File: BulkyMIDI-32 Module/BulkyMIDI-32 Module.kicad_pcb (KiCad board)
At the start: 2 copper layers, 100 x 100 mm, 47 parts, among them IC1 OLED, J1 DC IN, J2 MIDI OUT, J3 MIDI IN, J4 Faceplate, J5 MIDI THRU, J6 Serial, J7 Conn_Extras, J8 Module_Panel, M1 Mounting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

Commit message: Type C patched
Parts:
- added C2: 100nF, Capacitor_SMD:C_0805_2012Metric, F.Cu at (101.7, 64.9)
- added C7: 100nF, Capacitor_SMD:C_0805_2012Metric, F.Cu at (103.9, 74.4)
- added C8: 100nF, Capacitor_SMD:C_0805_2012Metric, F.Cu at (98.3, 64.9)
- added J9: USB_C_Receptacle_USB2.0, Connector_USB:USB_C_Receptacle_XKB_U262-16XN-4BVC11, F.Cu at (105.2, 58.5)
- C1, C3, C4: footprint Capacitor_THT:C_Rect_L7.0mm_W2.0mm_P5.00mm -> Capacitor_SMD:C_0805_2012Metric
- D1: value 1N4148 -> 1N4148WS; footprint Diode_THT:D_DO-35_SOD27_P7.62mm_Horizontal -> Diode_SMD:D_SOD-323
- R1, R2, R3, R4, R5, R6, R7: footprint Resistor_THT:R_Axial_DIN0207_L6.3mm_D2.5mm_P10.16mm_Horizontal -> Resistor_SMD:R_0805_2012Metric
- U1: footprint Package_DIP:DIP-14_W7.62mm -> Package_SO:SO-14_3.9x8.65mm_P1.27mm
- moved R7 9.40 mm to (113.3, 136.9)
- moved U1 8.57 mm to (159.8, 79.4)
- moved D1 1.52 mm to (132.7, 82.3)
- moved C3 1.02 mm to (120.0, 78.5)
- moved R1 0.89 mm to (167.0, 63.8)
- moved C4 0.83 mm to (109.2, 74.5)
- moved C1 0.38 mm to (149.6, 77.5)
- turned R3 to 0 degrees
- turned R4 to 0 degrees
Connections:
- A1 pad 18: (no net) -> unconnected-(A1-GPIO24-Pad18)
- A1 pad 19: (no net) -> unconnected-(A1-MOSI0/GPIO10-Pad19)
- A1 pad 21: (no net) -> unconnected-(A1-MISO0/GPIO9-Pad21)
- A1 pad 22: (no net) -> unconnected-(A1-GPIO25-Pad22)
- A1 pad 23: (no net) -> unconnected-(A1-SCLK0/GPIO11-Pad23)
- A1 pad 24: (no net) -> unconnected-(A1-~{CE0}/GPIO8-Pad24)
- A1 pad 26: (no net) -> unconnected-(A1-~{CE1}/GPIO7-Pad26)
- A1 pad 27: (no net) -> unconnected-(A1-ID_SD/GPIO0-Pad27)
- A1 pad 28: (no net) -> unconnected-(A1-ID_SC/GPIO1-Pad28)
- A1 pad 29: (no net) -> unconnected-(A1-GCLK1/GPIO5-Pad29)
- A1 pad 31: (no net) -> unconnected-(A1-GCLK2/GPIO6-Pad31)
- A1 pad 32: (no net) -> unconnected-(A1-PWM0/GPIO12-Pad32)
- A1 pad 33: (no net) -> unconnected-(A1-PWM1/GPIO13-Pad33)
- A1 pad 36: (no net) -> unconnected-(A1-GPIO16-Pad36)
- A1 pad 37: (no net) -> unconnected-(A1-GPIO26-Pad37)
- A1 pad 38: (no net) -> unconnected-(A1-GPIO20/MOSI1-Pad38)
- A2 pad 11: (no net) -> unconnected-(A2-A3V3-Pad11)
- A2 pad 12: (no net) -> unconnected-(A2-FMT-Pad12)
- A2 pad 13: (no net) -> unconnected-(A2-XSMT-Pad13)
- A2 pad 14: (no net) -> unconnected-(A2-DEMP-Pad14)
- A2 pad 15: (no net) -> unconnected-(A2-FLT-Pad15)
- J2 pad 1: (no net) -> unconnected-(J2-Pad1)
- J2 pad 3: (no net) -> unconnected-(J2-Pad3)
- J3 pad 1: (no net) -> unconnected-(J3-Pad1)
- J3 pad 2: (no net) -> unconnected-(J3-Pad2)
- J3 pad 3: (no net) -> unconnected-(J3-Pad3)
- J3 pad 6: Net-(J3-Pad6) -> unconnected-(J3-Pad6)
- J4 pad 5: (no net) -> unconnected-(J4-Pin_5-Pad5)
- J5 pad 1: (no net) -> unconnected-(J5-Pad1)
- J5 pad 3: (no net) -> unconnected-(J5-Pad3)
- J7 pad 16: (no net) -> unconnected-(J7-N.C.-Pad16)
- J7 pad 5: (no net) -> unconnected-(J7-N.C.-Pad5)
- J7 pad 6: (no net) -> unconnected-(J7-N.C.-Pad6)
- J7 pad 7: (no net) -> unconnected-(J7-N.C.-Pad7)
- J7 pad 8: (no net) -> unconnected-(J7-N.C.-Pad8)
- U1 pad 10: (no net) -> unconnected-(U1-Pad10)
- U1 pad 12: (no net) -> unconnected-(U1-Pad12)
- U2 pad 3: (no net) -> unconnected-(U2-Pad3)
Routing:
- net GND: track 11.6 -> 41.1 mm, vias 2 -> 11
- net +5V: track 178.1 -> 205.7 mm, vias 1 -> 2
- net Net-(D1-K): track 13.8 -> 30.5 mm, vias 0 -> 2
- net Net-(J5-Pad5): track 6.35 -> 18.3 mm, vias 0 -> 2
- net unconnected-(J3-Pad6): track 0.00 -> 10.0 mm
- net Net-(J3-Pad6): track 10.0 -> 0.00 mm
- net Net-(J8-PWR): track 4.08 -> 12.6 mm, vias 0 -> 2
- net Net-(J2-Pad4): track 14.8 -> 7.68 mm
- net Net-(D1-A): track 22.8 -> 29.3 mm
- net Net-(J5-Pad4): track 21.7 -> 16.4 mm, vias 0 -> 2
- net MIDI_THRUn: track 85.2 -> 90.3 mm
- net Net-(R1-Pad2): track 16.3 -> 21.0 mm, vias 0 -> 2
- net +3V3: track 299.0 -> 301.4 mm
- net PI_RX: track 128.3 -> 130.6 mm, vias 5 -> 8
- net PI_TX: track 87.5 -> 89.2 mm, vias 3 -> 4
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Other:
- net class Default removed
- net class Power removed

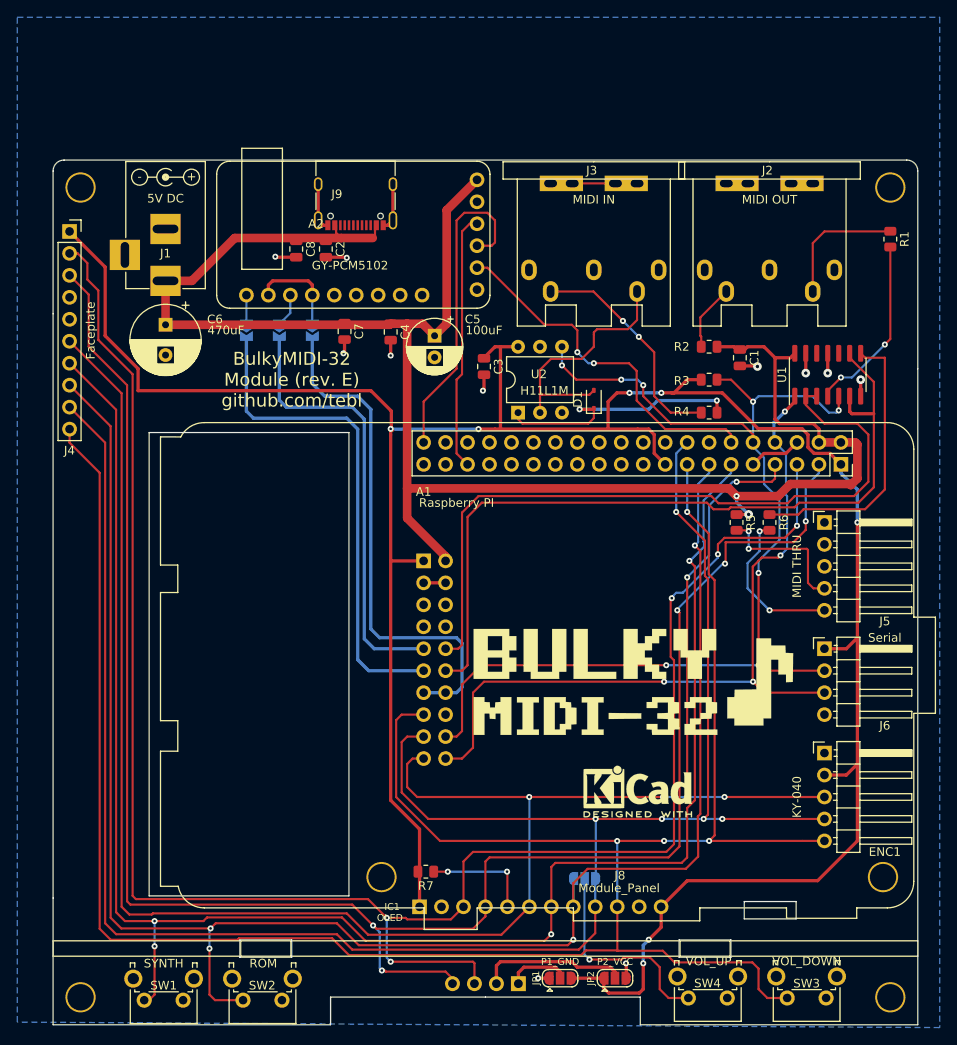
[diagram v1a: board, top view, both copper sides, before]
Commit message: Compact and integrated DAC with both MT32Pi and Dexed support
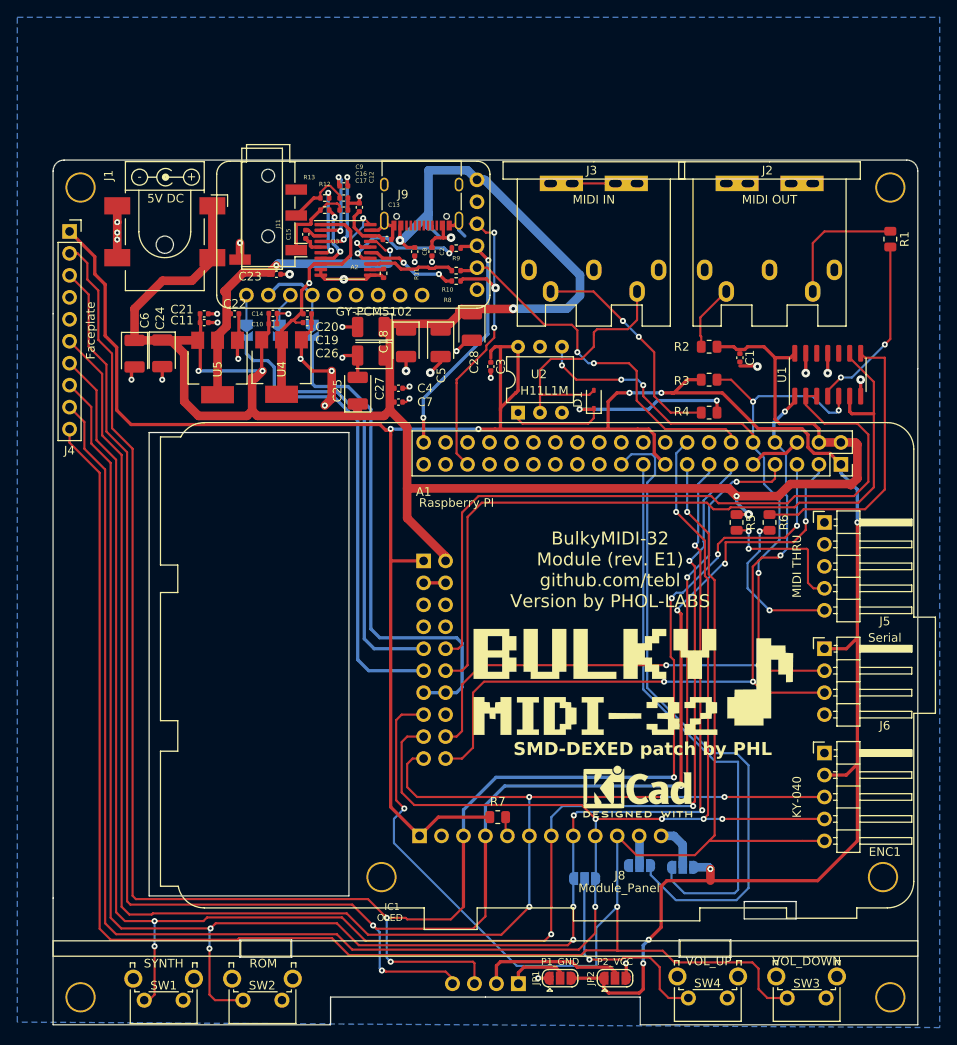
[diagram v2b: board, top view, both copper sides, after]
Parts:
- added C10: 10u, Capacitor_SMD:C_0402_1005Metric, F.Cu at (95.6, 73.5)
- added C11: 10u, Capacitor_SMD:C_0402_1005Metric, F.Cu at (87.7, 73.4)
- added C12: 2u2, Capacitor_SMD:C_0402_1005Metric, F.Cu at (105.6, 60.1)
- added C13: 100n, Capacitor_SMD:C_0402_1005Metric, F.Cu at (108.8, 63.8)
- added C14: 100n, Capacitor_SMD:C_0402_1005Metric, F.Cu at (95.6, 72.3)
- added C15: 2u2, Capacitor_SMD:C_0402_1005Metric, F.Cu at (99.4, 63.2)
- added C16: 2n2, Capacitor_SMD:C_0402_1005Metric, F.Cu at (103.8, 59.0)
- added C17: 2n2, Capacitor_SMD:C_0402_1005Metric, F.Cu at (103.8, 60.4)
- added C18: 100u, Capacitor_Tantalum_SMD:CP_EIA-3528-21_Kemet-B, F.Cu at (111.0, 75.8)
- added C19: 10u, Capacitor_SMD:C_0402_1005Metric, F.Cu at (99.6, 73.4)
- added C20: 100n, Capacitor_SMD:C_0402_1005Metric, F.Cu at (99.6, 72.4)
- added C21: 100n, Capacitor_SMD:C_0402_1005Metric, F.Cu at (87.7, 72.4)
- added C22: 100n, Capacitor_SMD:C_0402_1005Metric, F.Cu at (91.2, 72.4)
- added C23: 10u, Capacitor_SMD:C_0402_1005Metric, F.Cu at (96.0, 67.8)
- added C24: 100u, Capacitor_Tantalum_SMD:CP_EIA-3528-21_Kemet-B, F.Cu at (82.8, 77.0)
- added C25: 100u, Capacitor_Tantalum_SMD:CP_EIA-3528-21_Kemet-B, F.Cu at (105.4, 81.3)
- added C26: 100uF, Capacitor_Tantalum_SMD:CP_EIA-3528-21_Kemet-B, F.Cu at (106.9, 73.9)
- added C27: 100uF, Capacitor_Tantalum_SMD:CP_EIA-3528-21_Kemet-B, F.Cu at (106.9, 77.2)
- added C28: 100uF, Capacitor_Tantalum_SMD:CP_EIA-3528-21_Kemet-B, F.Cu at (118.6, 73.9)
- added C9: 2u2, Capacitor_SMD:C_0402_1005Metric, F.Cu at (103.8, 57.6)
- added J11: AudioJack4, Connector_Audio:Jack_3.5mm_PJ320D_Horizontal, F.Cu at (95.0, 61.2)
- added JP7: P1_GND, Jumper:SolderJumper-3_P1.3mm_Open_RoundedPad1.0x1.5mm, B.Cu at (138.0, 136.2)
- added JP8: P1_GND, Jumper:SolderJumper-3_P1.3mm_Open_RoundedPad1.0x1.5mm, B.Cu at (143.0, 136.4)
- added R10: 22, Resistor_SMD:R_0402_1005Metric, F.Cu at (116.8, 67.4)
- added R11: 22, Resistor_SMD:R_0402_1005Metric, F.Cu at (108.4, 67.7)
- added R12: 470, Resistor_SMD:R_0402_1005Metric, F.Cu at (101.6, 59.0)
- added R13: 470, Resistor_SMD:R_0402_1005Metric, F.Cu at (101.6, 60.4)
- added R8: 22, Resistor_SMD:R_0402_1005Metric, F.Cu at (116.8, 68.6)
- added R9: 22, Resistor_SMD:R_0402_1005Metric, F.Cu at (116.8, 64.8)
- added U3: PCM5102A, Package_SO:TSSOP-20_4.4x6.5mm_P0.65mm, F.Cu at (104.0, 65.0)
- added U4: AMS1117-3.3, Package_TO_SOT_SMD:SOT-223-3_TabPin2, F.Cu at (96.6, 78.5)
- added U5: AMS1117-3.3, Package_TO_SOT_SMD:SOT-223-3_TabPin2, F.Cu at (89.2, 78.6)
- C1, C2, C3, C4, C7, C8: footprint Capacitor_SMD:C_0805_2012Metric -> Capacitor_SMD:C_0402_1005Metric
- C5: footprint Capacitor_THT:CP_Radial_D6.3mm_P2.50mm -> Capacitor_Tantalum_SMD:CP_EIA-3528-21_Kemet-B
- C6: value 470uF -> 100u; footprint Capacitor_THT:CP_Radial_D8.0mm_P3.50mm -> Capacitor_Tantalum_SMD:CP_EIA-3528-21_Kemet-B
- J1: footprint BulkyMIDI-32:BARREL_JACK -> Connector_BarrelJack:BarrelJack_CLIFF_FC681465S_SMT_Horizontal
- moved C8 13.7 mm to (112.0, 65.2)
- moved C2 12.3 mm to (114.0, 65.2)
- moved R7 10.4 mm to (121.6, 130.6)
- moved C7 10.3 mm to (110.1, 82.6), turned to 0 degrees
- moved J9 7.64 mm to (112.8, 58.5)
- moved C4 6.57 mm to (110.1, 81.0), turned to 0 degrees
- moved J1 5.68 mm to (83.1, 62.9)
- moved C6 4.90 mm to (79.6, 77.0)
- moved C5 1.12 mm to (115.0, 75.8)
- moved C3 0.78 mm to (120.8, 78.5)
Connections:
- A1 pad 18: unconnected-(A1-GPIO24-Pad18) -> SW_DOWN_DEXED
- A1 pad 19: unconnected-(A1-MOSI0/GPIO10-Pad19) -> ENC_CLK_DEXED
- A1 pad 21: unconnected-(A1-MISO0/GPIO9-Pad21) -> ENC_DAT_DEXED
- A1 pad 23: unconnected-(A1-SCLK0/GPIO11-Pad23) -> ENC_SW_DEXED
- J8 pad 11: GND -> Net-(JP7-C)
- J8 pad 12: +3V3 -> Net-(JP8-C)
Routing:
- net +5V: track 205.7 -> 282.2 mm, vias 2 -> 7
- net ENC_DAT_DEXED: track 0.00 -> 75.4 mm
- net ENC_CLK_DEXED: track 0.00 -> 65.2 mm
- net GND: track 41.1 -> 95.2 mm, vias 11 -> 33
- net +3.3VP: track 0.00 -> 44.2 mm, vias 0 -> 3
- net +3.3VA: track 0.00 -> 29.2 mm, vias 0 -> 1
- net SW_DOWN: track 265.8 -> 283.1 mm, vias 4 -> 3
- net +3V3: track 301.4 -> 316.5 mm, vias 7 -> 8
- net Net-(U3-DIN): track 0.00 -> 14.7 mm, vias 0 -> 2
- net Net-(U3-CAPM): track 0.00 -> 11.2 mm, vias 0 -> 2
- net Net-(U3-LRCK): track 0.00 -> 10.8 mm, vias 0 -> 2
- net Net-(J8-PWR): track 12.6 -> 2.26 mm, vias 2 -> 0
- net Net-(U3-BCK): track 0.00 -> 10.1 mm
- net /AUDIO_L: track 0.00 -> 9.88 mm
- net Net-(U3-CAPP): track 0.00 -> 9.71 mm, vias 0 -> 2
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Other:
- board text added: "BulkyMIDI-32 Module (rev. E1) github.com/tebl Version by PHOL-LABS"
- board text added: "SMD-DEXED patch by PHL"
- board text removed: "BulkyMIDI-32 Module (rev. E) github.com/tebl"
